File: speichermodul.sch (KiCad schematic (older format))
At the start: 65 parts, among them IC1 6116, P1 CONN_3X2, P2 CONN_01X01, P3 CONN_01X01, P4 CONN_01X01, P5 CONN_01X01, P6 CONN_01X01, P7 CONN_01X01, P8 CONN_02X10, P9 CONN_02X10, SW1 SW_PUSH, SW2 SW_PUSH, U1 7400, U2 74LS08, U3 74LS08, U4 74LS14, U5 74LS540, U6 74LS540

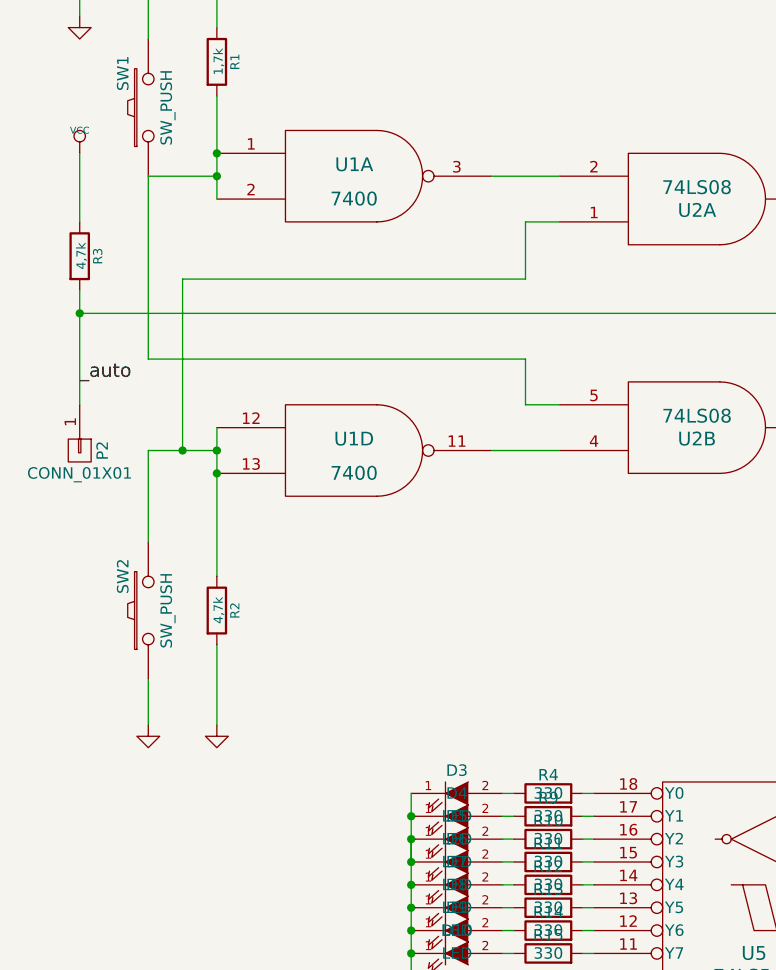
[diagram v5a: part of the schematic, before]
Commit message: Speicher Footprints
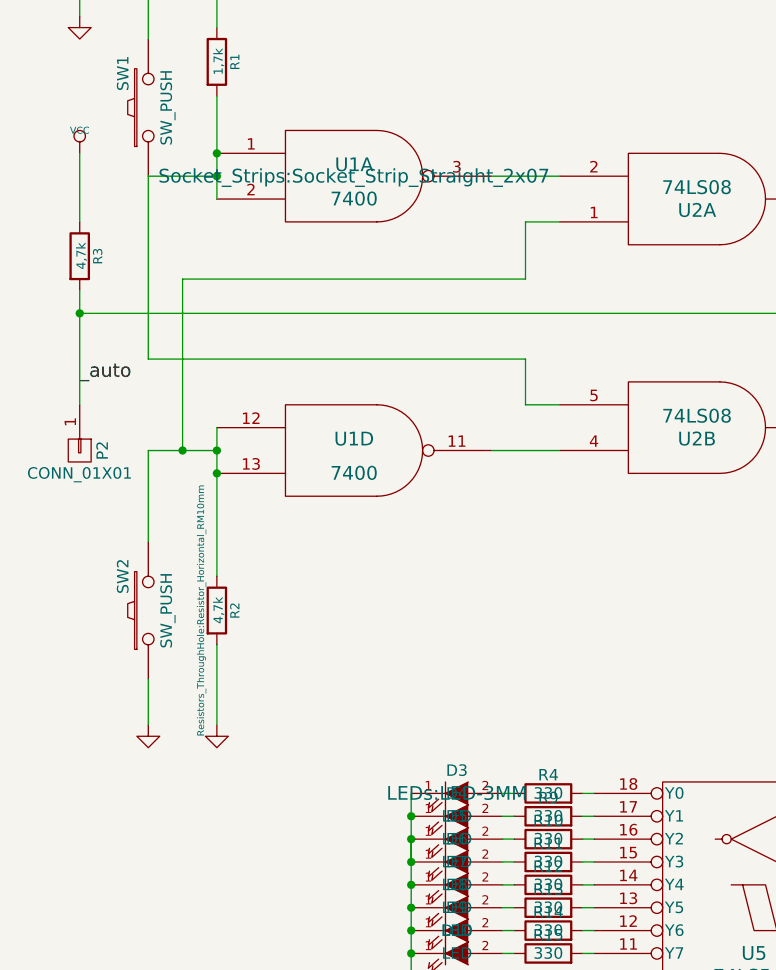
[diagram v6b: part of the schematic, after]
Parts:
- R2: footprint Discret:R3 -> Resistors_ThroughHole:Resistor_Horizontal_RM10mm
- U1: footprint (none) -> Socket_Strips:Socket_Strip_Straight_2x07
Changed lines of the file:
@@
 F 0 "U1" H 1900 3000 60  0000 C CNN
 F 1 "7400" H 1900 2850 60  0000 C CNN
-F 2 "" H 1900 2950 60  0001 C CNN
+F 2 "Socket_Strips:Socket_Strip_Straight_2x07" H 1900 2950 60  0000 C CNN
 F 3 "~" H 1900 2950 60  0000 C CNN
 	1    1900 2950
@@
 F 0 "R2" V 1380 4850 40  0000 C CNN
 F 1 "4,7k" V 1307 4851 40  0000 C CNN
-F 2 "Discret:R3" V 1230 4850 30  0001 C CNN
+F 2 "Resistors_ThroughHole:Resistor_Horizontal_RM10mm" V 1230 4850 30  0000 C CNN
 F 3 "~" H 1300 4850 30  0000 C CNN
 	1    1300 4850
@@
 F 0 "D3" H 2350 5750 50  0000 C CNN
 F 1 "LED" H 2350 5550 50  0000 C CNN
-F 2 "LEDs:LED-3MM" H 2350 5650 60  0001 C CNN
+F 2 "LEDs:LED-3MM" H 2350 5650 60  0000 C CNN
 F 3 "" H 2350 5650 60  0000 C CNN
 	1    2350 5650

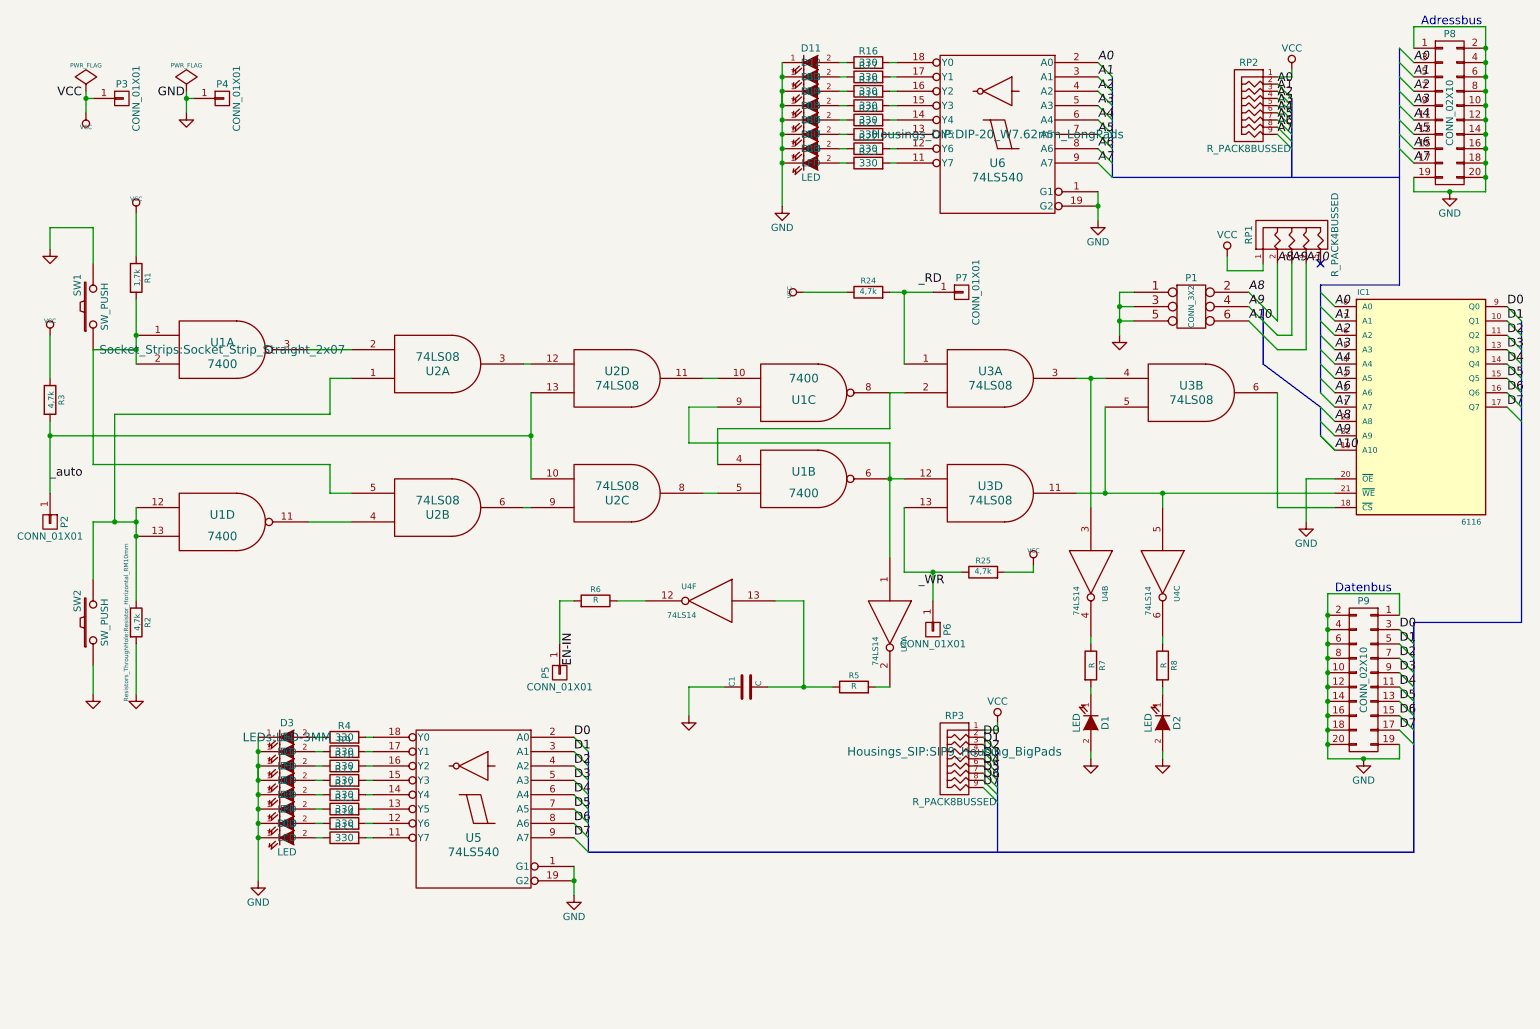
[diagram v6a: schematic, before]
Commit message: einige DIPs hinzugefügt
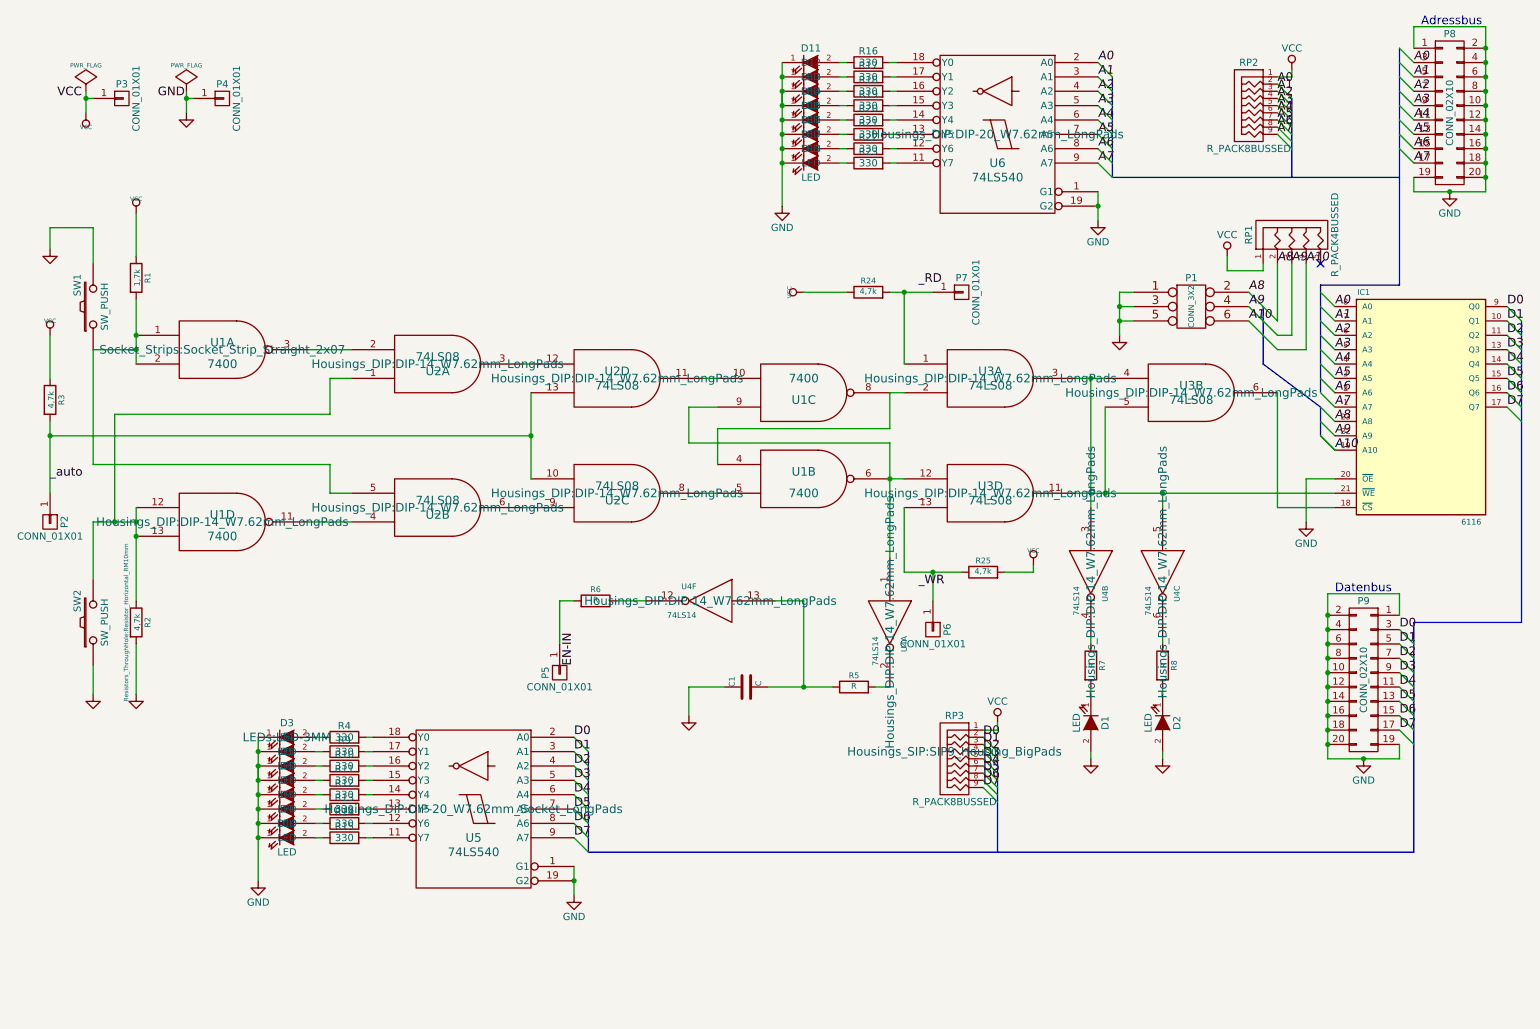
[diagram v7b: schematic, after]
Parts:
- U1, U2, U3, U4: footprint (none) -> Housings_DIP:DIP-14_W7.62mm_LongPads
- U5: footprint Housings_DIP:DIP-20_W7.62mm_LongPads -> Housings_DIP:DIP-20_W7.62mm_Socket_LongPads
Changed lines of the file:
@@
 F 0 "U2" H 3400 3100 60  0000 C CNN
 F 1 "74LS08" H 3400 3000 60  0000 C CNN
-F 2 "" H 3400 3050 60  0001 C CNN
+F 2 "Housings_DIP:DIP-14_W7.62mm_LongPads" H 3400 3050 60  0000 C CNN
 F 3 "~" H 3400 3050 60  0000 C CNN
 	1    3400 3050
@@
 F 0 "U2" H 3400 4100 60  0000 C CNN
 F 1 "74LS08" H 3400 4000 60  0000 C CNN
-F 2 "" H 3400 4050 60  0001 C CNN
+F 2 "Housings_DIP:DIP-14_W7.62mm_LongPads" H 3400 4050 60  0000 C CNN
 F 3 "~" H 3400 4050 60  0000 C CNN
 	2    3400 4050
@@
 F 0 "U2" H 4650 3200 60  0000 C CNN
 F 1 "74LS08" H 4650 3100 60  0000 C CNN
-F 2 "" H 4650 3150 60  0001 C CNN
+F 2 "Housings_DIP:DIP-14_W7.62mm_LongPads" H 4650 3150 60  0000 C CNN
 F 3 "~" H 4650 3150 60  0000 C CNN
 	4    4650 3150
@@
 F 0 "U2" H 4650 4000 60  0000 C CNN
 F 1 "74LS08" H 4650 3900 60  0000 C CNN
-F 2 "" H 4650 3950 60  0001 C CNN
+F 2 "Housings_DIP:DIP-14_W7.62mm_LongPads" H 4650 3950 60  0000 C CNN
 F 3 "~" H 4650 3950 60  0000 C CNN
 	3    4650 3950
@@
 F 0 "U1" H 1900 4200 60  0000 C CNN
 F 1 "7400" H 1900 4050 60  0000 C CNN
-F 2 "" H 1900 4150 60  0001 C CNN
+F 2 "Housings_DIP:DIP-14_W7.62mm_LongPads" H 1900 4150 60  0000 C CNN
 F 3 "~" H 1900 4150 60  0000 C CNN
 	4    1900 4150
@@
 F 0 "U3" H 7250 3200 60  0000 C CNN
 F 1 "74LS08" H 7250 3100 60  0000 C CNN
-F 2 "" H 7250 3150 60  0001 C CNN
+F 2 "Housings_DIP:DIP-14_W7.62mm_LongPads" H 7250 3150 60  0000 C CNN
 F 3 "~" H 7250 3150 60  0000 C CNN
 	1    7250 3150
@@
 F 0 "U3" H 8650 3300 60  0000 C CNN
 F 1 "74LS08" H 8650 3200 60  0000 C CNN
-F 2 "" H 8650 3250 60  0001 C CNN
+F 2 "Housings_DIP:DIP-14_W7.62mm_LongPads" H 8650 3250 60  0000 C CNN
 F 3 "~" H 8650 3250 60  0000 C CNN
 	2    8650 3250
@@
 F 0 "U3" H 7250 4000 60  0000 C CNN
 F 1 "74LS08" H 7250 3900 60  0000 C CNN
-F 2 "" H 7250 3950 60  0001 C CNN
+F 2 "Housings_DIP:DIP-14_W7.62mm_LongPads" H 7250 3950 60  0000 C CNN
 F 3 "~" H 7250 3950 60  0000 C CNN
 	4    7250 3950
@@
 F 0 "U4" H 6700 4950 40  0000 C CNN
 F 1 "74LS14" H 6750 4750 40  0000 C CNN
-F 2 "" H 6550 4850 60  0001 C CNN
+F 2 "Housings_DIP:DIP-14_W7.62mm_LongPads" H 6550 4850 60  0000 C CNN
 F 3 "~" H 6550 4850 60  0000 C CNN
 	1    6550 4850
@@
 F 0 "U4" H 5450 4800 40  0000 C CNN
 F 1 "74LS14" H 5500 4600 40  0000 C CNN
-F 2 "" H 5300 4700 60  0001 C CNN
+F 2 "Housings_DIP:DIP-14_W7.62mm_LongPads" H 5300 4700 60  0000 C CNN
 F 3 "~" H 5300 4700 60  0000 C CNN
 	6    5300 4700
@@
 F 0 "U4" H 8100 4600 40  0000 C CNN
 F 1 "74LS14" H 8150 4400 40  0000 C CNN
-F 2 "" H 7950 4500 60  0001 C CNN
+F 2 "Housings_DIP:DIP-14_W7.62mm_LongPads" H 7950 4500 60  0000 C CNN
 F 3 "~" H 7950 4500 60  0000 C CNN
 	2    7950 4500
@@
 F 0 "U4" H 8600 4600 40  0000 C CNN
 F 1 "74LS14" H 8650 4400 40  0000 C CNN
-F 2 "" H 8450 4500 60  0001 C CNN
+F 2 "Housings_DIP:DIP-14_W7.62mm_LongPads" H 8450 4500 60  0000 C CNN
 F 3 "~" H 8450 4500 60  0000 C CNN
 	3    8450 4500
@@
 F 0 "U5" H 3650 5950 60  0000 C CNN
 F 1 "74LS540" H 3650 5850 60  0000 C CNN
-F 2 "Housings_DIP:DIP-20_W7.62mm_LongPads" H 3650 6150 60  0001 C CNN
+F 2 "Housings_DIP:DIP-20_W7.62mm_Socket_LongPads" H 3650 6150 60  0000 C CNN
 F 3 "" H 3650 6150 60  0000 C CNN
 	1    3650 6150

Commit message: einige Rewistoren hinzugefügt
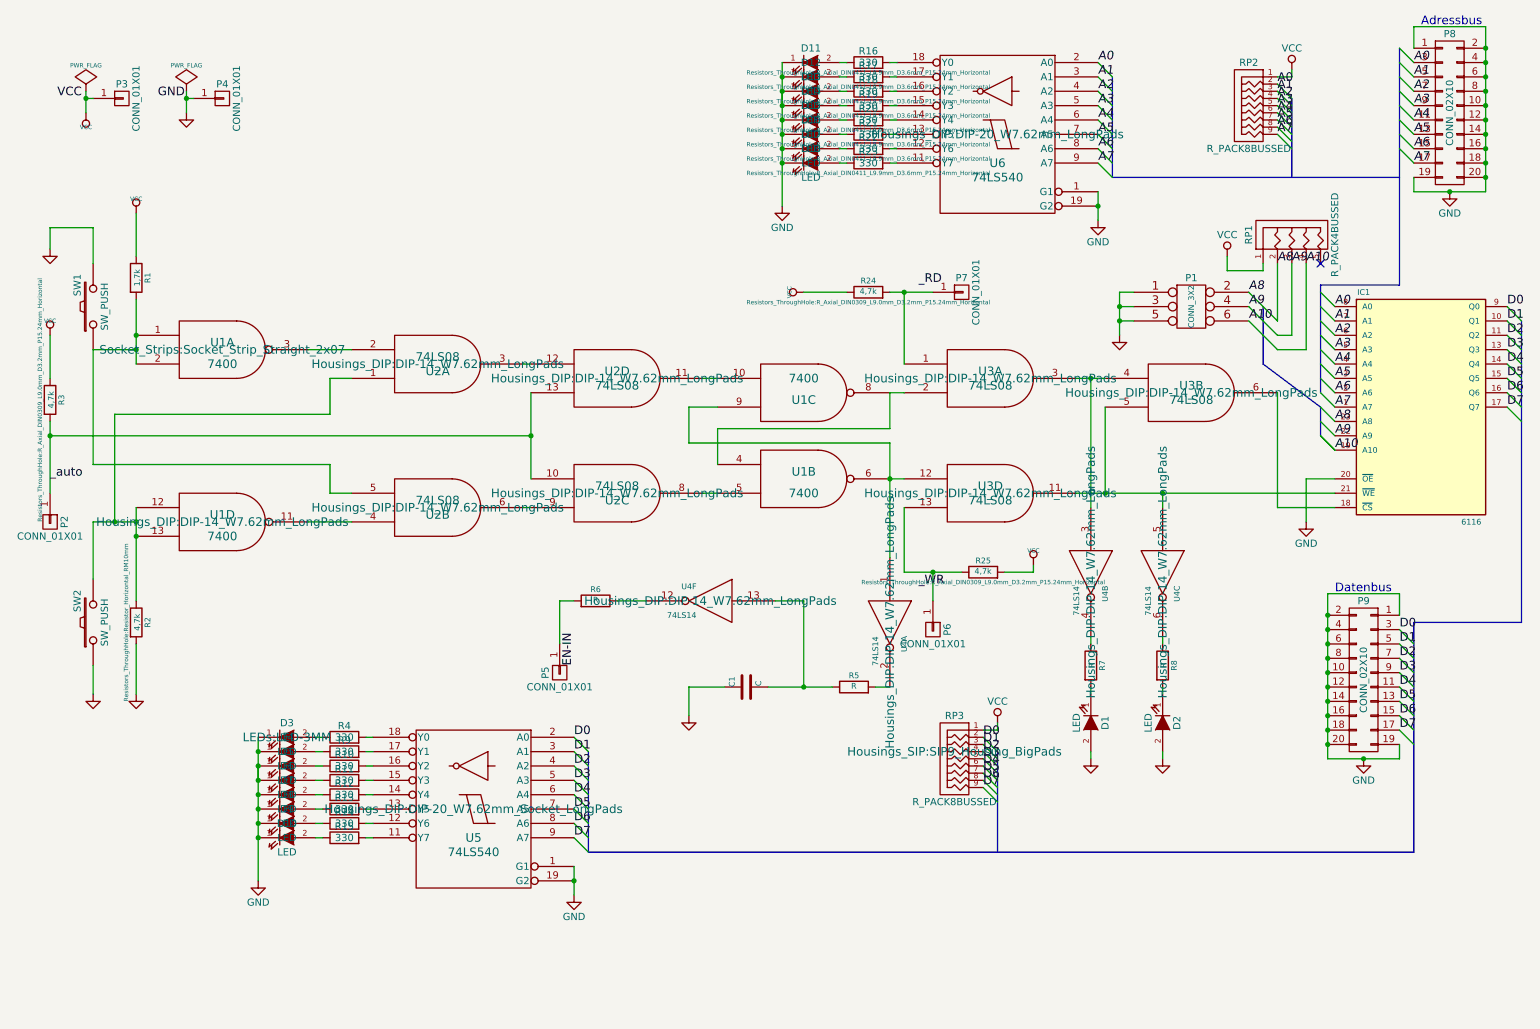
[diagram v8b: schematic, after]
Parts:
- R16, R17, R18, R19, R20, R21, R22, R23: footprint (none) -> Resistors_ThroughHole:R_Axial_DIN0411_L9.9mm_D3.6mm_P15.24mm_Horizontal
- R24, R25, R3: footprint (none) -> Resistors_ThroughHole:R_Axial_DIN0309_L9.0mm_D3.2mm_P15.24mm_Horizontal
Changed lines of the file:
@@
 F 0 "R3" V 780 3300 40  0000 C CNN
 F 1 "4,7k" V 707 3301 40  0000 C CNN
-F 2 "" V 630 3300 30  0001 C CNN
+F 2 "Resistors_ThroughHole:R_Axial_DIN0309_L9.0mm_D3.2mm_P15.24mm_Horizontal" V 630 3300 30  0000 C CNN
 F 3 "~" H 700 3300 30  0000 C CNN
 	1    700  3300
@@
 F 0 "R24" V 6480 2550 40  0000 C CNN
 F 1 "4,7k" V 6407 2551 40  0000 C CNN
-F 2 "" V 6330 2550 30  0001 C CNN
+F 2 "Resistors_ThroughHole:R_Axial_DIN0309_L9.0mm_D3.2mm_P15.24mm_Horizontal" V 6330 2550 30  0000 C CNN
 F 3 "~" H 6400 2550 30  0000 C CNN
 	1    6400 2550
@@
 F 0 "R25" V 7280 4500 40  0000 C CNN
 F 1 "4,7k" V 7207 4501 40  0000 C CNN
-F 2 "" V 7130 4500 30  0001 C CNN
+F 2 "Resistors_ThroughHole:R_Axial_DIN0309_L9.0mm_D3.2mm_P15.24mm_Horizontal" V 7130 4500 30  0000 C CNN
 F 3 "~" H 7200 4500 30  0000 C CNN
 	1    7200 4500
@@
 F 0 "R16" V 6480 950 50  0000 C CNN
 F 1 "330" V 6400 950 50  0000 C CNN
-F 2 "" V 6330 950 30  0001 C CNN
+F 2 "Resistors_ThroughHole:R_Axial_DIN0411_L9.9mm_D3.6mm_P15.24mm_Horizontal" V 6330 950 30  0000 C CNN
 F 3 "" H 6400 950 30  0000 C CNN
 	1    6400 950
@@
 F 0 "R17" V 6480 1050 50  0000 C CNN
 F 1 "330" V 6400 1050 50  0000 C CNN
-F 2 "" V 6330 1050 30  0001 C CNN
+F 2 "Resistors_ThroughHole:R_Axial_DIN0411_L9.9mm_D3.6mm_P15.24mm_Horizontal" V 6330 1050 30  0000 C CNN
 F 3 "" H 6400 1050 30  0000 C CNN
 	1    6400 1050
@@
 F 0 "R18" V 6480 1150 50  0000 C CNN
 F 1 "330" V 6400 1150 50  0000 C CNN
-F 2 "" V 6330 1150 30  0001 C CNN
+F 2 "Resistors_ThroughHole:R_Axial_DIN0411_L9.9mm_D3.6mm_P15.24mm_Horizontal" V 6330 1150 30  0000 C CNN
 F 3 "" H 6400 1150 30  0000 C CNN
 	1    6400 1150
@@
 F 0 "R19" V 6480 1250 50  0000 C CNN
 F 1 "330" V 6400 1250 50  0000 C CNN
-F 2 "" V 6330 1250 30  0001 C CNN
+F 2 "Resistors_ThroughHole:R_Axial_DIN0411_L9.9mm_D3.6mm_P15.24mm_Horizontal" V 6330 1250 30  0000 C CNN
 F 3 "" H 6400 1250 30  0000 C CNN
 	1    6400 1250
@@
 F 0 "R20" V 6480 1350 50  0000 C CNN
 F 1 "330" V 6400 1350 50  0000 C CNN
-F 2 "" V 6330 1350 30  0001 C CNN
+F 2 "Resistors_ThroughHole:R_Axial_DIN0411_L9.9mm_D3.6mm_P15.24mm_Horizontal" V 6330 1350 30  0000 C CNN
 F 3 "" H 6400 1350 30  0000 C CNN
 	1    6400 1350
-	0    -1   -1   0
-$EndComp
-$Comp
-L R R21
-U 1 1 57D5BBB8
-P 6400 1450
-F 0 "R21" V 6480 1450 50  0000 C CNN
-F 1 "330" V 6400 1450 50  0000 C CNN
-F 2 "" V 6330 1450 30  0001 C CNN
-F 3 "" H 6400 1450 30  0000 C CNN
-	1    6400 1450
 	0    -1   -1   0
 $EndComp
@@
 F 0 "R22" V 6480 1550 50  0000 C CNN
 F 1 "330" V 6400 1550 50  0000 C CNN
-F 2 "" V 6330 1550 30  0001 C CNN
+F 2 "Resistors_ThroughHole:R_Axial_DIN0411_L9.9mm_D3.6mm_P15.24mm_Horizontal" V 6330 1550 30  0000 C CNN
 F 3 "" H 6400 1550 30  0000 C CNN
 	1    6400 1550
@@
 F 0 "R23" V 6480 1650 50  0000 C CNN
 F 1 "330" V 6400 1650 50  0000 C CNN
-F 2 "" V 6330 1650 30  0001 C CNN
+F 2 "Resistors_ThroughHole:R_Axial_DIN0411_L9.9mm_D3.6mm_P15.24mm_Horizontal" V 6330 1650 30  0000 C CNN
 F 3 "" H 6400 1650 30  0000 C CNN
 	1    6400 1650
@@
 Text Label 9250 1450 0    60   ~ 0
 A7
+$Comp
+L R R21
+U 1 1 57D5BBB8
+P 6400 1450
+F 0 "R21" V 6480 1450 50  0000 C CNN
+F 1 "330" V 6400 1450 50  0000 C CNN
+F 2 "Resistors_ThroughHole:R_Axial_DIN0411_L9.9mm_D3.6mm_P15.24mm_Horizontal" V 6330 1450 30  0000 C CNN
+F 3 "" H 6400 1450 30  0000 C CNN
+	1    6400 1450
+	0    -1   -1   0
+$EndComp
 $EndSCHEMATC
